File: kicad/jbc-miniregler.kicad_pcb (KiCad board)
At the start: 2 copper layers, 110 x 100 mm, 156 parts, among them J1 ActivEnergy B2+, J2 ActivEnergy B1+, J3 Makita Plus, J4 Makita Plus, J5 Makita Minus, J6 Makita Minus, J7 ActivEnergy B2-, J8 ActivEnergy B1-, J9 SWD, Q1 2N7002, Q2 MMBT3904, Q3 MMBT3904, Q4 ZXMP10A13FTA, Q5 KND3508A, SW1 UP, SW2 DOWN, SW3 ENTER, SW4 BACK, SW5 Ein/Aus, SW6 RESET, U1 OLED-128x32-Module, U2 XL7005A, U3 XL7005A, U4 MAX3232, U5 YD3082EESA, U6 Pico, U7 TL431, U8 PN7006A, U9 GS8332-SR, X1 POWER, X2 COM, X3 Lötkolben, X4 GND-Öse

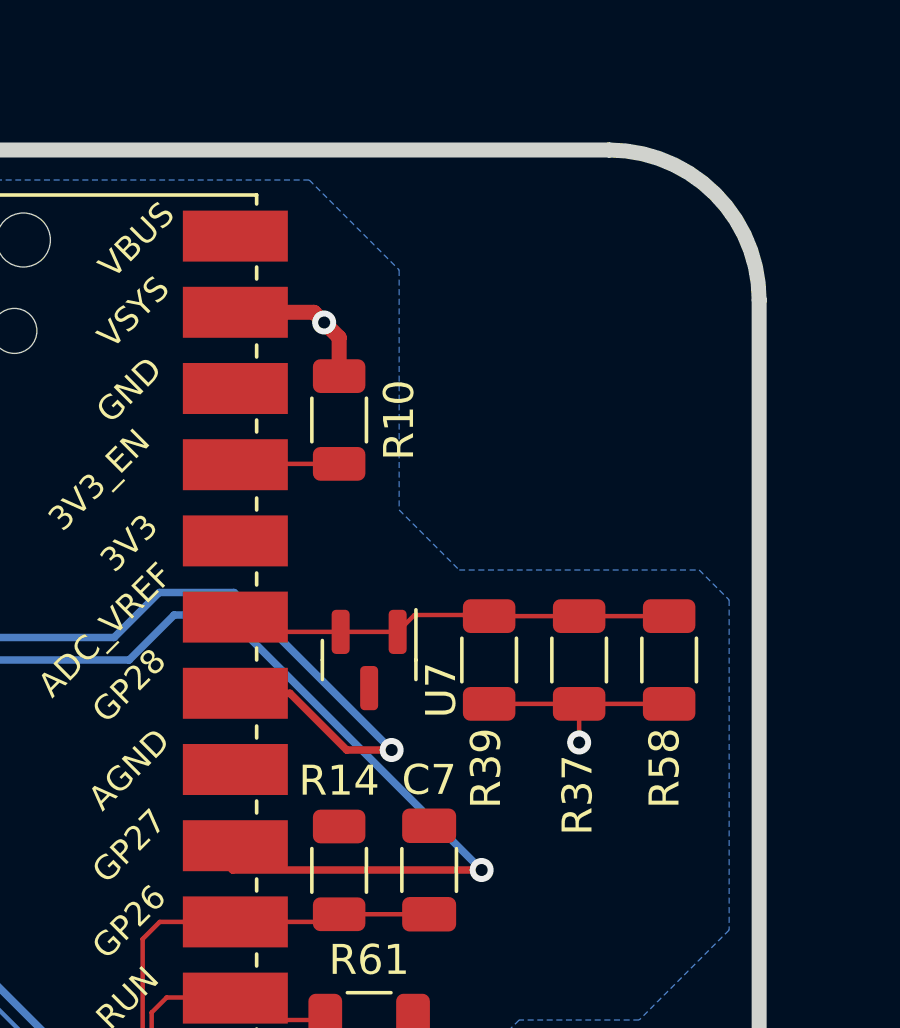
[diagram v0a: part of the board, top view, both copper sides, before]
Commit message: BOM auf Lieferbarkeit aktualisiert, TODO: DRC bereinigen
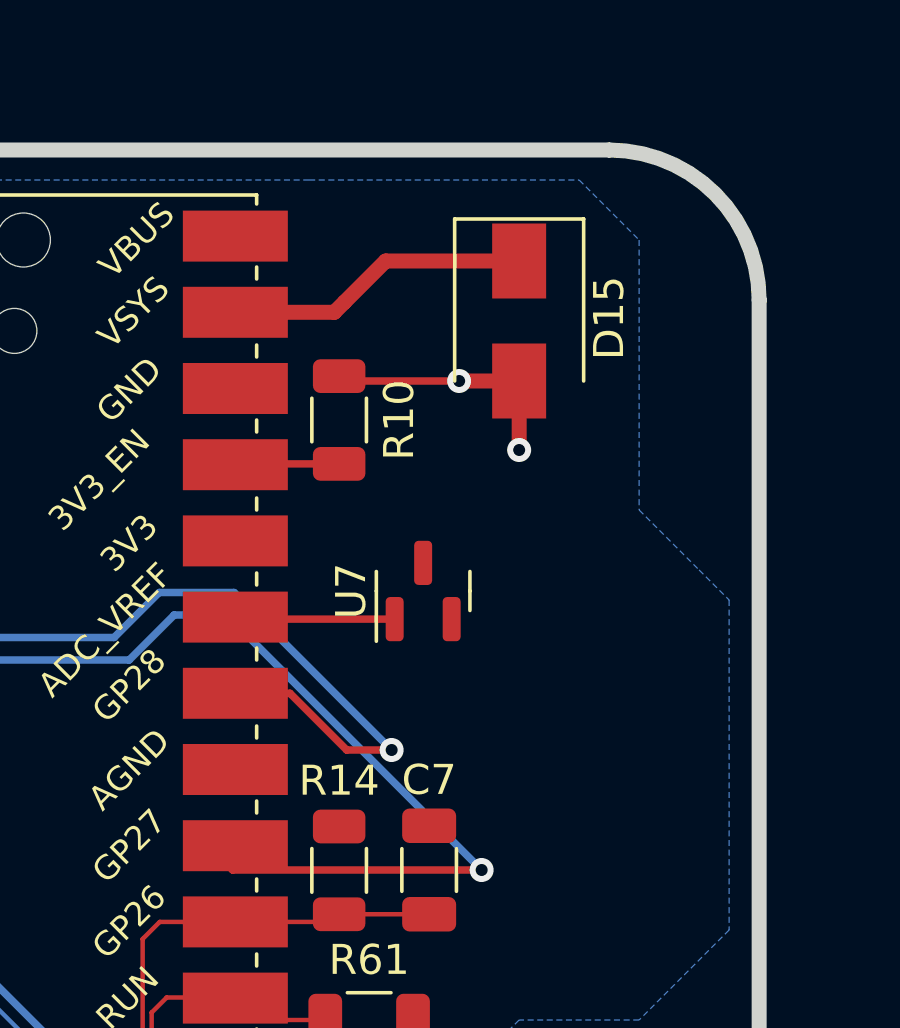
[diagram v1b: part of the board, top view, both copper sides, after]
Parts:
- removed R37, R39, R58: 1k, Resistor_SMD:R_1206_3216Metric
- added D15: SS210, htl_smd:D_SMA_wide, F.Cu at (193.0, 48.7)
- C1, C16, C17, C18, C19, C2, C20, C21, C22, C25, C27, C3, C4: value 100n -> 100n/50V
- C10, C14: value 33n -> 33n/50V
- C26, C28, C29, C6: value 10n -> 10n/50V
- R24: value 6k1 -> 6k2
- U7: value TL431 -> LM4040CIM3-3.0/NOPB
- U8: value PN7006A -> TF2101M-TAH
- moved U7 2.92 mm to (189.8, 57.7), turned to 90 degrees
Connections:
- net Net-(R10-Pad1) renamed /Arduino/3V3_EN
- net Net-(R61-Pad2) renamed /Arduino/RUN
- U6 pad 35: Net-(R37-Pad2) -> /Arduino/VREF
- U6 pad 39: +3.3V -> /Arduino/VSYS
- U7 pad 1: Net-(R37-Pad2) -> /Arduino/VREF
- U7 pad 2: Net-(R37-Pad2) -> GND
- U7 pad 3: GND -> (no net)
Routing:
- net Net-(R37-Pad2): track 15.8 -> 0.00 mm
- net /Arduino/VSYS: track 0.00 -> 11.1 mm
- net /Arduino/VREF: track 0.00 -> 6.93 mm
- net +3.3V: track 256.8 -> 251.9 mm

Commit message: DRC bereinigt
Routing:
- net /Arduino/VREF: track 6.93 -> 6.24 mm
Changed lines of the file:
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@@
   (segment (start 141.07 106.68) (end 142.25 105.5) (width 0.15) (layer "B.Cu") (net 108))
   (segment (start 159.3755 98) (end 159.5 98.1245) (width 0.15) (layer "B.Cu") (net 108))
-  (segment (start 183.1325 59.0625) (end 182.64 58.57) (width 0.15) (layer "F.Cu") (net 109))
   (segment (start 182.7075 58.6375) (end 182.64 58.57) (width 0.25) (layer "F.Cu") (net 109))
   (segment (start 188.85 58.6375) (end 182.7075 58.6375) (width 0.25) (layer "F.Cu") (net 109))

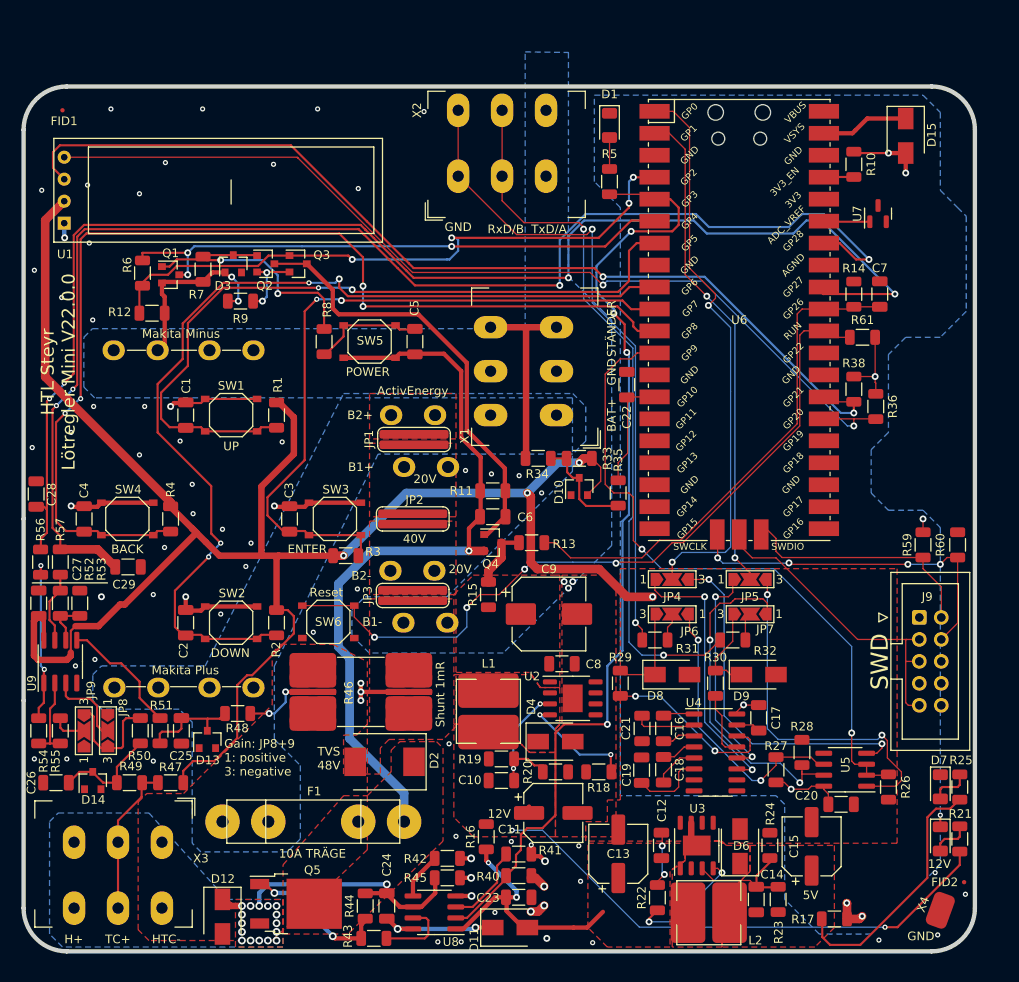
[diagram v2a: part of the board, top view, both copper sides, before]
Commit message: PCB fertig. Platzierung verbessert (Federklemme unter OLED)
Layout minimal verbessert
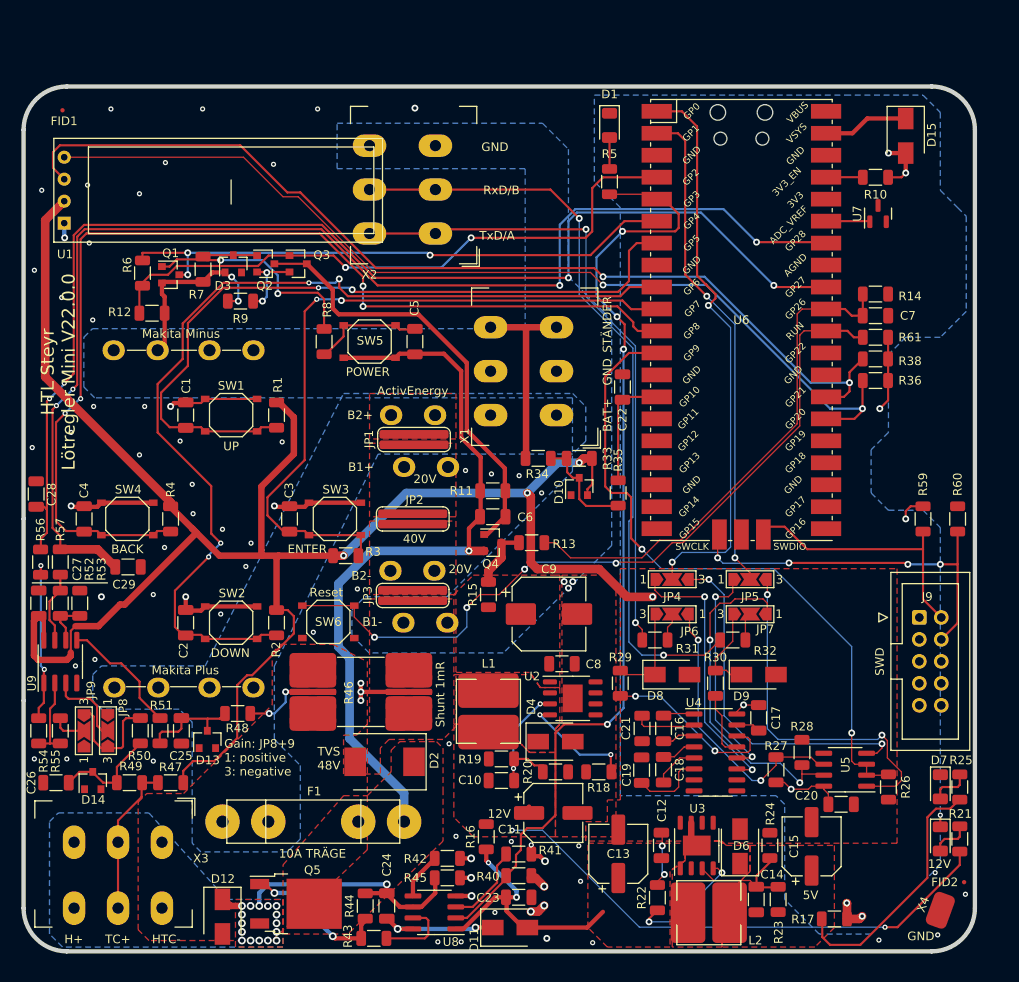
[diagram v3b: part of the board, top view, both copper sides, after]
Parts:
- moved X2 17.6 mm to (131.0, 60.0), turned to 90 degrees
- moved R38 4.30 mm to (189.5, 74.5), turned to 180 degrees
- moved R36 3.00 mm to (189.5, 77.0), turned to 180 degrees
- moved R59 3.00 mm to (195.0, 93.0)
- moved R60 3.00 mm to (199.0, 93.0)
- moved R10 2.92 mm to (189.5, 53.5), turned to 0 degrees
- moved C7 2.55 mm to (189.5, 69.5), turned to 0 degrees
- moved R14 2.50 mm to (189.5, 67.0), turned to 0 degrees
- moved R61 1.50 mm to (189.5, 72.0)
- moved C22 0.57 mm to (160.2, 77.8)
- moved U6 0.25 mm to (174.0, 70.0)
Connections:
- net Net-(J9-Pad2) renamed /Arduino/SWDIO
- net Net-(J9-Pad4) renamed /Arduino/SWCLK
- J9 pad 3: Net-(J9-Pad3) -> GND
- J9 pad 5: Net-(J9-Pad3) -> GND
- J9 pad 9: Net-(J9-Pad3) -> GND
- U6 pad 42: Net-(J9-Pad3) -> GND
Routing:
- net Net-(J9-Pad3): track 38.1 -> 0.00 mm
- net /Arduino/Temperatur: track 157.1 -> 138.7 mm
- net /Arduino/Strom: track 156.3 -> 142.8 mm
- net /Arduino/SWCLK: track 42.3 -> 51.7 mm
- net /UART RS232/RS485/RxD_B: track 83.6 -> 89.3 mm
- net /Arduino/TxD: track 64.5 -> 66.7 mm
- net GND: track 61.2 -> 63.3 mm, vias 72 -> 71
- net /Arduino/RUN: track 88.1 -> 89.7 mm
- net /Arduino/SWDIO: track 28.9 -> 30.3 mm
- net +3.3V: track 251.9 -> 250.5 mm
- net /Arduino/BACK: track 123.8 -> 122.5 mm
- net /Arduino/SDA: track 112.3 -> 113.6 mm
- net /Arduino/3V3_EN: track 4.37 -> 5.15 mm
- net /Arduino/Batteriemessung: track 59.0 -> 59.7 mm
- net /Arduino/SCL: track 115.3 -> 116.0 mm
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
